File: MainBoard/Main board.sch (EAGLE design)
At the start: 3 parts

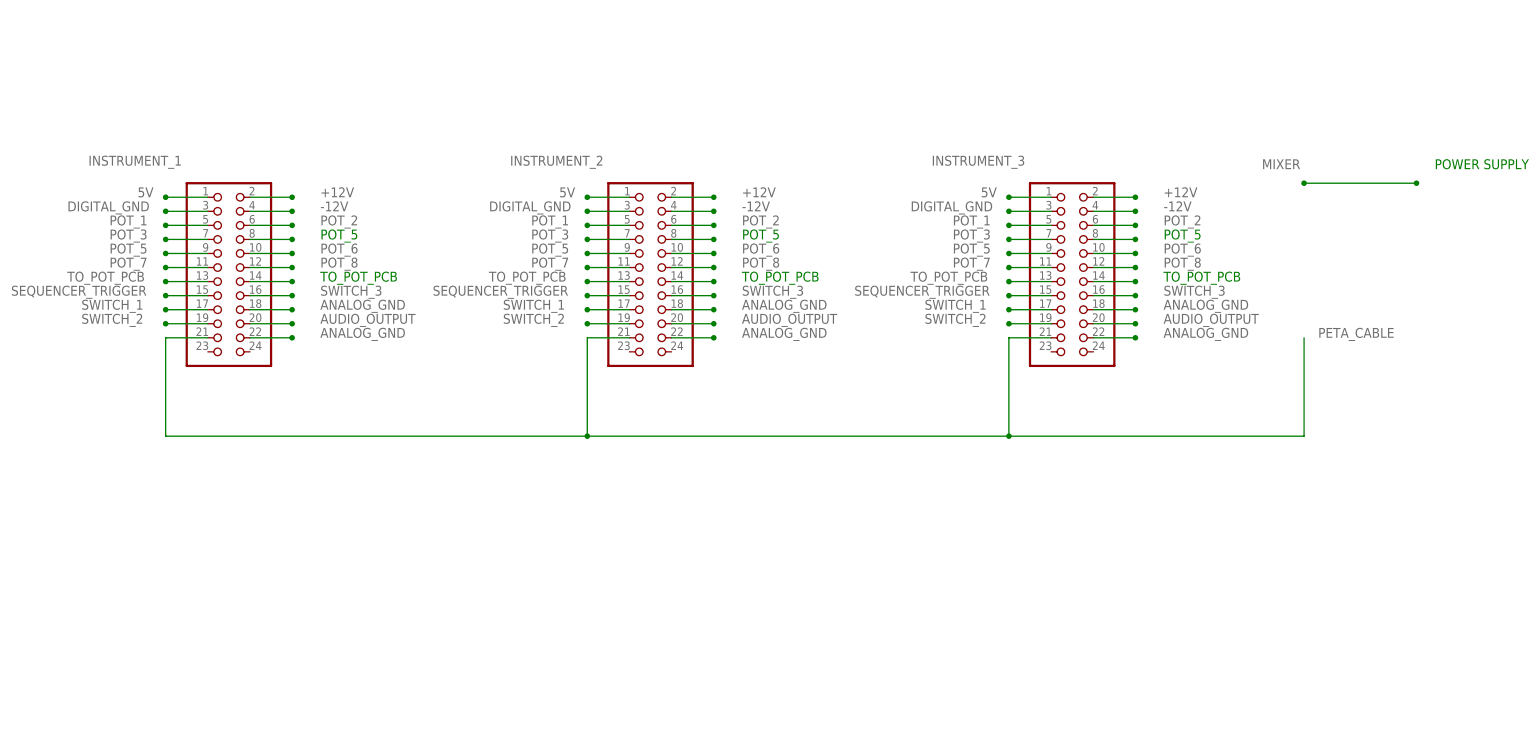
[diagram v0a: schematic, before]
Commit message: Update Main board.sch
Updated pinouts. Need feedback.
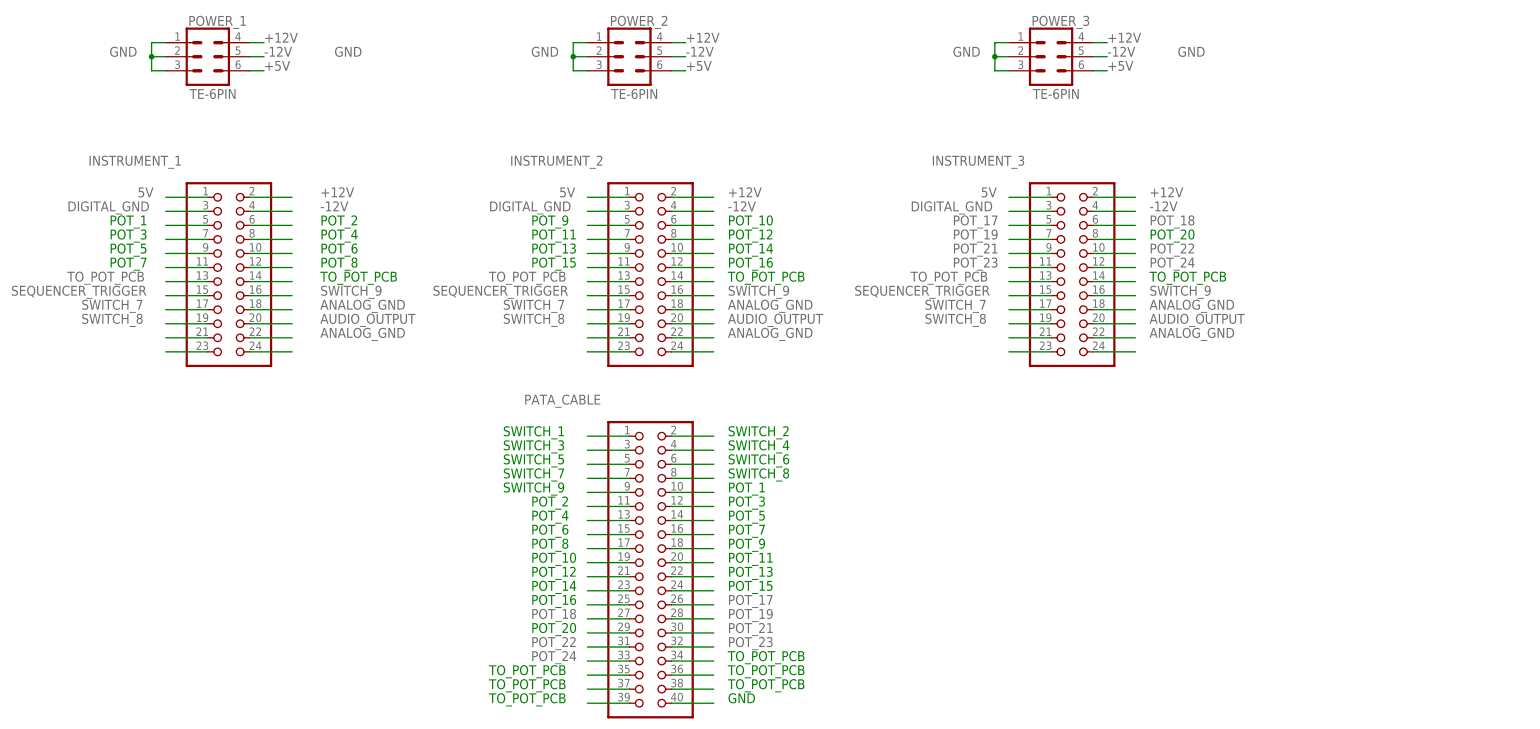
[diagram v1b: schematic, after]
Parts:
- added PATA_CABLE: (no value), pinhead:PINHD-2X20/90
- added POWER_1, POWER_2, POWER_3: TE-6PIN, Capstone:TE-6PIN
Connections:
- net POT_1 renamed POT_17
- net POT_2 renamed POT_18
- net POT_3 renamed POT_19
- net POT_5 renamed POT_21
- net POT_6 renamed POT_22
- net POT_7 renamed POT_23
- net POT_8 renamed POT_24
- net SWITCH_1 renamed SWITCH_7
- net SWITCH_2 renamed SWITCH_8
- net SWITCH_3 renamed SWITCH_9
- new net +5V: POWER_1.6, POWER_2.6, POWER_3.6
- new net GND: POWER_1.1, POWER_1.3, POWER_1.5, POWER_2.1, POWER_2.3, POWER_2.5, POWER_3.1, POWER_3.3, POWER_3.5
- new net N$10: PATA_CABLE.24
- new net N$11: PATA_CABLE.2
- new net N$12: PATA_CABLE.4
- new net N$13: PATA_CABLE.26
- new net N$15: PATA_CABLE.6
- new net N$16: PATA_CABLE.28
- new net N$17: PATA_CABLE.8
- new net N$19: PATA_CABLE.30
- new net N$20: PATA_CABLE.10
- new net N$21: PATA_CABLE.32
- new net N$22: PATA_CABLE.34
- new net N$23: PATA_CABLE.12
- new net N$25: PATA_CABLE.14
- new net N$26: PATA_CABLE.16
- new net N$27: PATA_CABLE.18
- new net N$28: PATA_CABLE.20
- new net N$29: PATA_CABLE.36
- new net N$30: PATA_CABLE.38
- new net N$31: PATA_CABLE.40
- new net N$32: PATA_CABLE.39
- new net N$33: PATA_CABLE.37
- new net N$34: PATA_CABLE.35
- new net N$35: PATA_CABLE.33
- new net N$36: PATA_CABLE.31
- new net N$37: PATA_CABLE.29
- new net N$38: PATA_CABLE.27
- new net N$39: PATA_CABLE.25
- new net N$40: PATA_CABLE.23
- new net N$41: PATA_CABLE.21
- new net N$42: PATA_CABLE.19
- new net N$43: PATA_CABLE.17
- new net N$44: PATA_CABLE.15
- new net N$45: PATA_CABLE.13
- new net N$46: PATA_CABLE.11
- new net N$47: PATA_CABLE.9
- new net N$48: PATA_CABLE.7
- new net N$49: PATA_CABLE.5
- new net N$50: PATA_CABLE.3
- new net N$51: PATA_CABLE.1
- new net N$52: INSTRUMENT_1.23
- new net N$53: INSTRUMENT_1.24
- new net N$54: INSTRUMENT_2.23
- new net N$55: INSTRUMENT_2.24
- new net N$56: INSTRUMENT_3.23
- new net N$57: INSTRUMENT_3.24
- new net N$7: INSTRUMENT_1.21
- new net N$8: INSTRUMENT_2.21
- new net N$9: PATA_CABLE.22
- net +12V: now also POWER_1.2, POWER_2.2, POWER_3.2
- net -12V: now also POWER_1.4, POWER_2.4, POWER_3.4
- net PETA_CABLE: no longer INSTRUMENT_1.21, INSTRUMENT_2.21
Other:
- note added: "GND"
- note added: "POT_1"
- note added: "POT_10"
- note added: "POT_11"
- note added: "POT_12"
- note added: "POT_13"
- note added: "POT_14"
- note added: "POT_15"
- note added: "POT_16"
- note added: "POT_2"
- note added: "POT_20"
- note added: "POT_3"
- note added: "POT_4"
- note added: "POT_6"
- note added: "POT_7"
- note added: "POT_8"
- note added: "POT_9"
- note added: "SWITCH_1"
- note added: "SWITCH_2"
- note added: "SWITCH_3"
- note added: "SWITCH_4"
- note added: "SWITCH_5"
- note added: "SWITCH_6"
- note added: "SWITCH_7"
- note added: "SWITCH_8"
- note added: "SWITCH_9"
- note removed: "POWER SUPPLY"

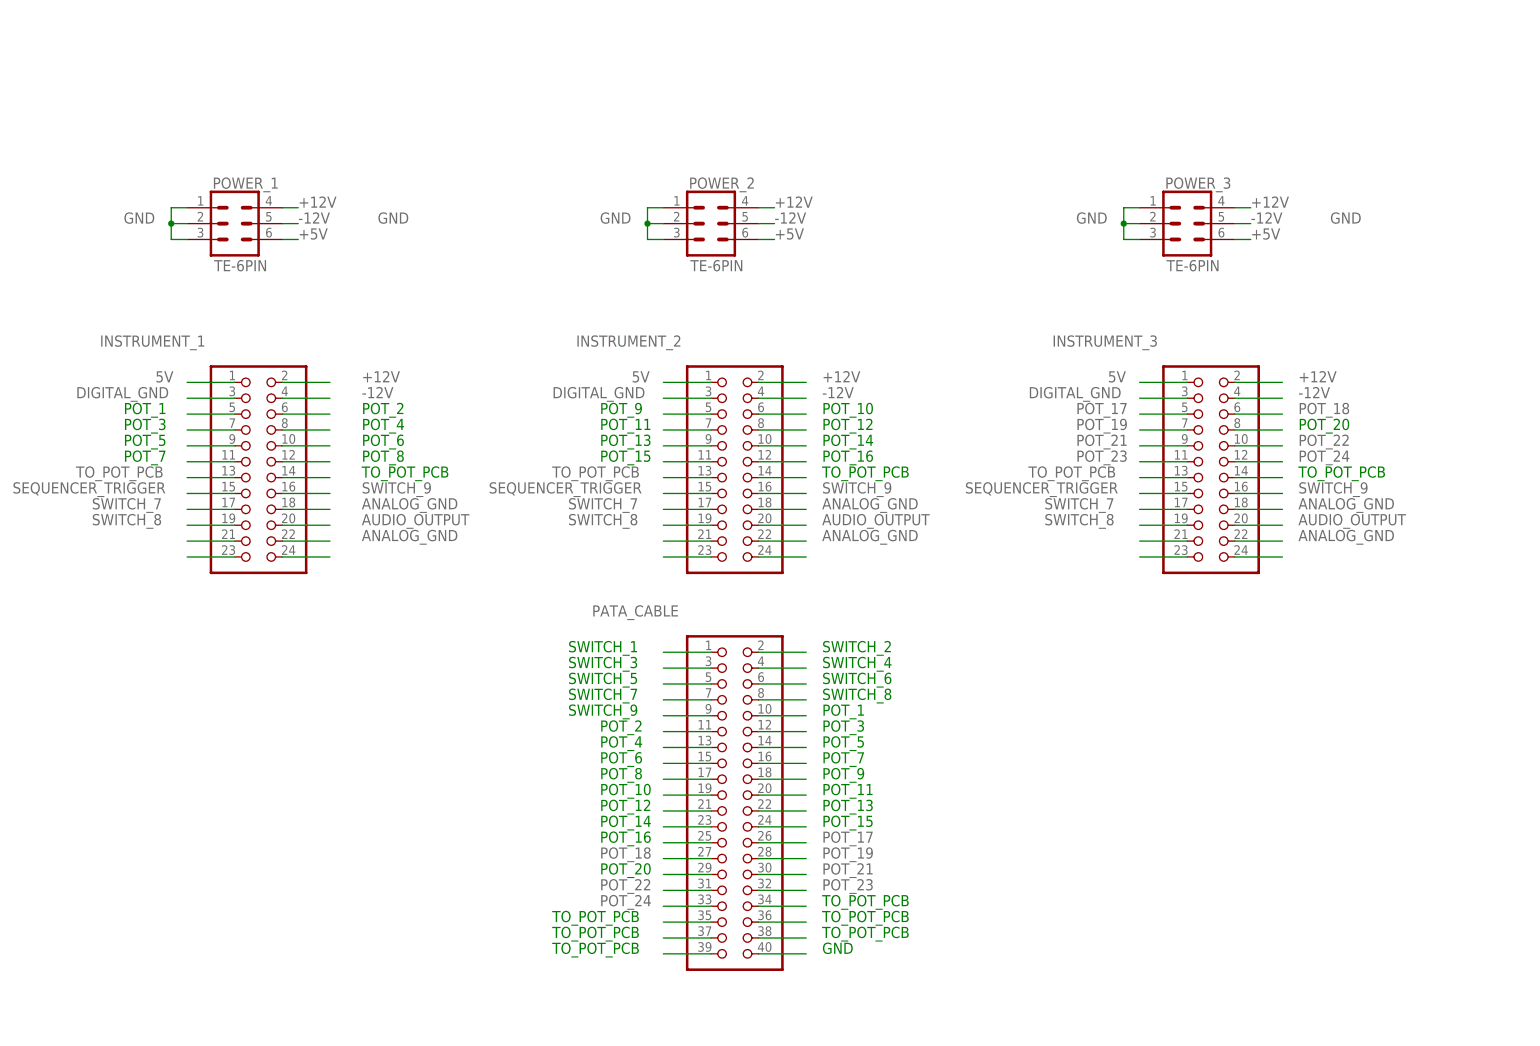
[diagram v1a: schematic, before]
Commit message: Update Main board.sch
Updated version with wiring.
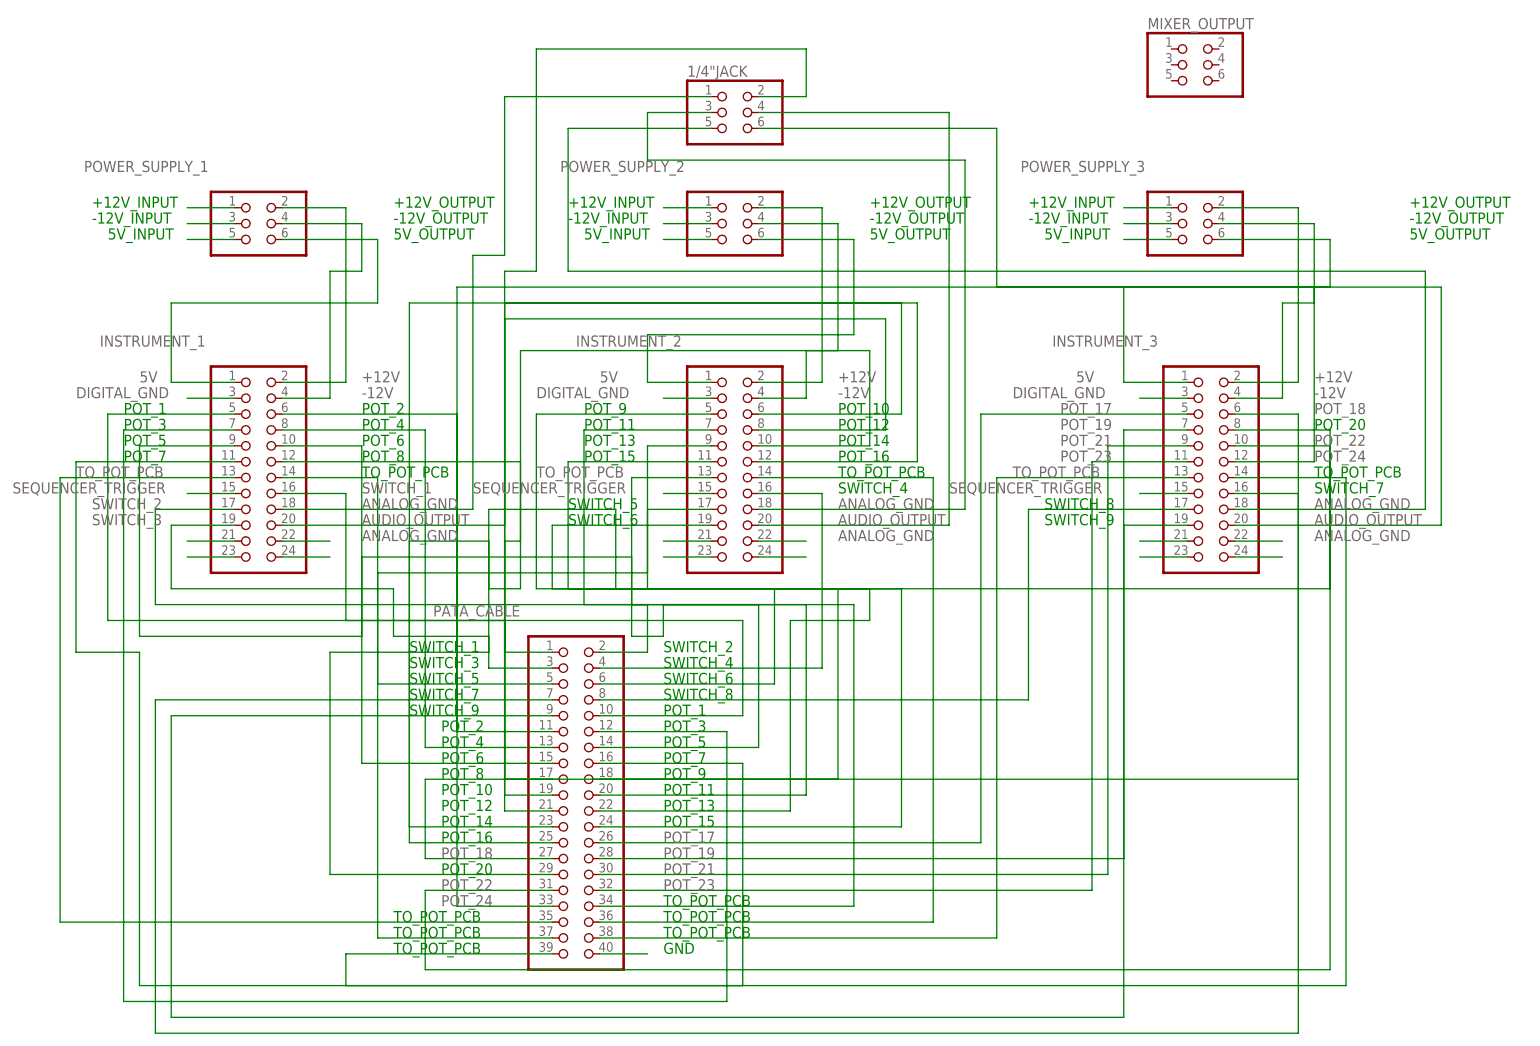
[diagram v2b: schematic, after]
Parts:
- removed POWER_1, POWER_2, POWER_3: TE-6PIN, Capstone:TE-6PIN
- added 1/4"JACK, MIXER_OUTPUT, POWER_SUPPLY_1, POWER_SUPPLY_2, POWER_SUPPLY_3: (no value), pinhead:PINHD-2X3/90
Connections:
- removed net +5V: POWER_1.6, POWER_2.6, POWER_3.6
- removed net GND: POWER_1.1, POWER_1.3, POWER_1.5, POWER_2.1, POWER_2.3, POWER_2.5, POWER_3.1, POWER_3.3, POWER_3.5
- removed net N$10: PATA_CABLE.24
- removed net N$11: PATA_CABLE.2
- removed net N$12: PATA_CABLE.4
- removed net N$13: PATA_CABLE.26
- removed net N$15: PATA_CABLE.6
- removed net N$16: PATA_CABLE.28
- removed net N$17: PATA_CABLE.8
- removed net N$19: PATA_CABLE.30
- removed net N$20: PATA_CABLE.10
- removed net N$21: PATA_CABLE.32
- removed net N$22: PATA_CABLE.34
- removed net N$23: PATA_CABLE.12
- removed net N$24: INSTRUMENT_1.8
- removed net N$25: PATA_CABLE.14
- removed net N$26: PATA_CABLE.16
- removed net N$27: PATA_CABLE.18
- removed net N$28: PATA_CABLE.20
- removed net N$29: PATA_CABLE.36
- removed net N$30: PATA_CABLE.38
- removed net N$32: PATA_CABLE.39
- removed net N$33: PATA_CABLE.37
- removed net N$34: PATA_CABLE.35
- removed net N$35: PATA_CABLE.33
- removed net N$36: PATA_CABLE.31
- removed net N$37: PATA_CABLE.29
- removed net N$38: PATA_CABLE.27
- removed net N$39: PATA_CABLE.25
- removed net N$40: PATA_CABLE.23
- removed net N$42: PATA_CABLE.19
- removed net N$43: PATA_CABLE.17
- removed net N$44: PATA_CABLE.15
- removed net N$46: PATA_CABLE.11
- removed net N$47: PATA_CABLE.9
- removed net N$48: PATA_CABLE.7
- removed net N$49: PATA_CABLE.5
- removed net N$50: PATA_CABLE.3
- removed net N$51: PATA_CABLE.1
- removed net N$6: INSTRUMENT_3.8
- removed net N$9: PATA_CABLE.22
- removed net SWITCH_7: INSTRUMENT_1.17, INSTRUMENT_2.17, INSTRUMENT_3.17
- removed net SWITCH_8: INSTRUMENT_1.19, INSTRUMENT_2.19, INSTRUMENT_3.19
- removed net SWITCH_9: INSTRUMENT_1.16, INSTRUMENT_2.16, INSTRUMENT_3.16
- new net N$58: POWER_SUPPLY_1.1
- new net N$59: POWER_SUPPLY_1.3
- new net N$60: POWER_SUPPLY_1.5
- new net N$64: POWER_SUPPLY_2.1
- new net N$65: POWER_SUPPLY_2.3
- new net N$66: POWER_SUPPLY_2.5
- new net N$70: POWER_SUPPLY_3.1
- new net N$71: POWER_SUPPLY_3.3
- new net N$72: POWER_SUPPLY_3.5
- new net SWITCH_1: INSTRUMENT_1.16, INSTRUMENT_2.16, INSTRUMENT_3.16, PATA_CABLE.1, PATA_CABLE.4, PATA_CABLE.7
- new net SWITCH_2: INSTRUMENT_1.17, INSTRUMENT_2.17, INSTRUMENT_3.17, PATA_CABLE.2, PATA_CABLE.5, PATA_CABLE.8
- new net SWITCH_3: INSTRUMENT_1.19, INSTRUMENT_2.19, INSTRUMENT_3.19, PATA_CABLE.3, PATA_CABLE.6, PATA_CABLE.9
- net +12V: now also POWER_SUPPLY_1.2, POWER_SUPPLY_2.2, POWER_SUPPLY_3.2; no longer POWER_1.2, POWER_2.2, POWER_3.2
- net -12V: now also POWER_SUPPLY_1.4, POWER_SUPPLY_2.4, POWER_SUPPLY_3.4; no longer POWER_1.4, POWER_2.4, POWER_3.4
- net 5V: now also POWER_SUPPLY_1.6, POWER_SUPPLY_2.6, POWER_SUPPLY_3.6
- net ANALOG_GND: now also 1/4"JACK.1, 1/4"JACK.3, 1/4"JACK.5
- net AUDIO_OUTPUT: now also 1/4"JACK.2, 1/4"JACK.4, 1/4"JACK.6
- net N$18: now also PATA_CABLE.37
- net N$2: now also PATA_CABLE.36
- net N$3: now also INSTRUMENT_3.8, PATA_CABLE.29; no longer INSTRUMENT_2.8
- net N$41: now also INSTRUMENT_2.8
- net N$45: now also INSTRUMENT_1.8
- net N$5: now also PATA_CABLE.39
- net POT_17: now also PATA_CABLE.10, PATA_CABLE.18, PATA_CABLE.26
- net POT_18: now also PATA_CABLE.11, PATA_CABLE.19, PATA_CABLE.27
- net POT_19: now also PATA_CABLE.12, PATA_CABLE.20, PATA_CABLE.28
- net POT_21: now also PATA_CABLE.14, PATA_CABLE.22, PATA_CABLE.30
- net POT_22: now also PATA_CABLE.15, PATA_CABLE.23, PATA_CABLE.31
- net POT_23: now also PATA_CABLE.16, PATA_CABLE.24, PATA_CABLE.32
- net POT_24: now also PATA_CABLE.17, PATA_CABLE.25, PATA_CABLE.33
- net TO_POT_PCB: now also PATA_CABLE.34, PATA_CABLE.35, PATA_CABLE.38
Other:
- note added: "+12V_INPUT"
- note added: "+12V_OUTPUT"
- note added: "-12V_INPUT"
- note added: "-12V_OUTPUT"
- note added: "5V_INPUT"
- note added: "5V_OUTPUT"
- moved on the sheet: PATA_CABLE
